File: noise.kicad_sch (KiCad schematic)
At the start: 23 parts, among them J2 Conn_01x04_Pin, SW1 SW_SP3T, U20 LF351N, U5 MM5837

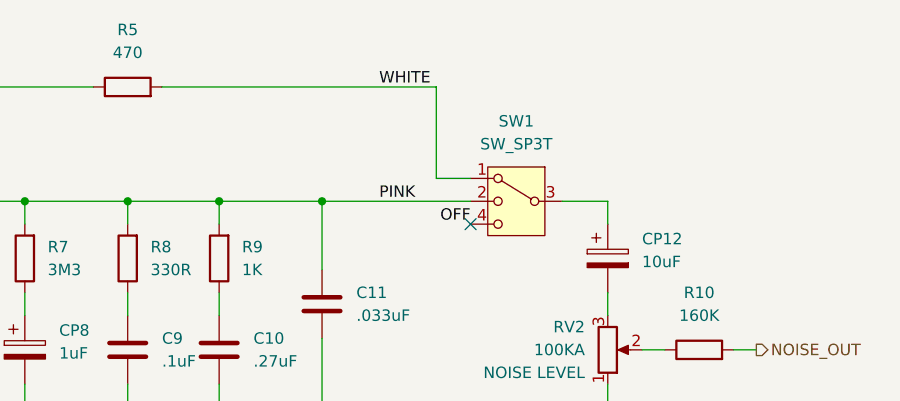
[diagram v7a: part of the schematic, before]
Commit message: Fix VCF layout, routing, adding pads for switches
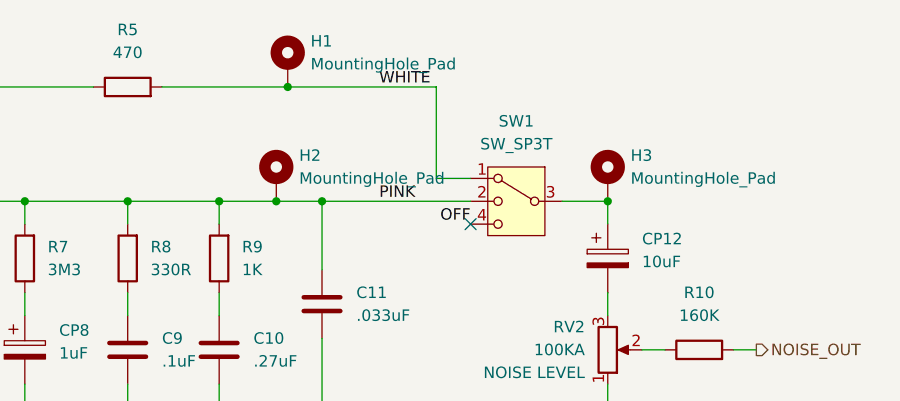
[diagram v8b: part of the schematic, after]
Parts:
- added H1, H2, H3: MountingHole_Pad, MountingHole:MountingHole_2.2mm_M2_Pad, symbol Mechanical:MountingHole_Pad
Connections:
- net PINK: now also H2.1
- net WHITE: now also H1.1
- net at CP12.1, SW1.3: now also H3.1
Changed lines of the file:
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@@
 	)
 	(junction
+		(at 160.02 87.63)
+		(diameter 0)
+		(color 0 0 0 0)
+	)
+	(junction
 		(at 101.6 77.47)
 		(diameter 0)
@@
 	)
 	(junction
+		(at 161.29 74.93)
+		(diameter 0)
+		(color 0 0 0 0)
+	)
+	(junction
 		(at 153.67 87.63)
 		(diameter 0)
@@
 	)
 	(junction
+		(at 196.85 87.63)
+		(diameter 0)
+		(color 0 0 0 0)
+	)
+	(junction
 		(at 132.08 87.63)
 		(diameter 0)
@@
 	(wire
 		(pts
+			(xy 160.02 87.63) (xy 165.1 87.63)
+		)
+		(stroke
+			(width 0)
+			(type default)
+		)
+	)
+	(wire
+		(pts
 			(xy 88.9 83.82) (xy 91.44 83.82)
 		)
@@
 	(wire
 		(pts
-			(xy 153.67 87.63) (xy 165.1 87.63)
+			(xy 153.67 87.63) (xy 160.02 87.63)
 		)
 		(stroke
@@
 	(wire
 		(pts
+			(xy 161.29 74.93) (xy 147.32 74.93)
+		)
+		(stroke
+			(width 0)
+			(type default)
+		)
+	)
+	(wire
+		(pts
 			(xy 143.51 97.79) (xy 143.51 100.33)
 		)
@@
 	(wire
 		(pts
-			(xy 177.8 74.93) (xy 147.32 74.93)
+			(xy 177.8 74.93) (xy 161.29 74.93)
 		)
 		(stroke
@@
 	)
 	(symbol
+		(lib_id "Mechanical:MountingHole_Pad")
+		(at 196.85 85.09 0)
+		(unit 1)
+		(exclude_from_sim no)
+		(in_bom no)
+		(on_board yes)
+		(dnp no)
+		(fields_autoplaced yes)
+		(property "Reference" "H3"
+			(at 199.39 82.5499 0)
+			(effects
+				(font
+					(size 1.27 1.27)
+				)
+				(justify left)
+			)
+		)
+		(property "Value" "MountingHole_Pad"
+			(at 199.39 85.0899 0)
+			(effects
+				(font
+					(size 1.27 1.27)
+				)
+				(justify left)
+			)
+		)
+		(property "Footprint" "MountingHole:MountingHole_2.2mm_M2_Pad"
+			(at 196.85 85.09 0)
+			(effects
+				(font
+					(size 1.27 1.27)
+				)
+				(hide yes)
+			)
+		)
+		(property "Datasheet" "~"
+			(at 196.85 85.09 0)
+			(effects
+				(font
+					(size 1.27 1.27)
+				)
+				(hide yes)
+			)
+		)
+		(property "Description" "Mounting Hole with connection"
+			(at 196.85 85.09 0)
+			(effects
+				(font
+					(size 1.27 1.27)
+				)
+				(hide yes)
+			)
+		)
+		(pin "1"
+		)
+		(instances
+			(project "jensx1000"
+				(path "/3c53febc-5769-4c45-8f8f-0aba2c04e944/23ff179f-f3ca-4876-91dc-9a0adb7dbeaf"
+					(reference "H3")
+					(unit 1)
+				)
+			)
+		)
+	)
+	(symbol
 		(lib_id "Switch:SW_SP3T")
 		(at 186.69 87.63 0)
@@
 					(unit 1)
 				)
+			)
+		)
+	)
+	(symbol
+		(lib_id "Mechanical:MountingHole_Pad")
+		(at 160.02 85.09 0)
+		(unit 1)
+		(exclude_from_sim no)
+		(in_bom no)
+		(on_board yes)
+		(dnp no)
+		(fields_autoplaced yes)
+		(property "Reference" "H2"
+			(at 162.56 82.5499 0)
+			(effects
+				(font
+					(size 1.27 1.27)
+				)
+				(justify left)
+			)
+		)
+		(property "Value" "MountingHole_Pad"
+			(at 162.56 85.0899 0)
+			(effects
+				(font
+					(size 1.27 1.27)
+				)
+				(justify left)
+			)
+		)
+		(property "Footprint" "MountingHole:MountingHole_2.2mm_M2_Pad"
+			(at 160.02 85.09 0)
+			(effects
+				(font
+					(size 1.27 1.27)
+				)
+				(hide yes)
+			)
+		)
+		(property "Datasheet" "~"
+			(at 160.02 85.09 0)
+			(effects
+				(font
+					(size 1.27 1.27)
+				)
+				(hide yes)
+			)
+		)
+		(property "Description" "Mounting Hole with connection"
+			(at 160.02 85.09 0)
+			(effects
+				(font
+					(size 1.27 1.27)
+				)
+				(hide yes)
+			)
+		)
+		(pin "1"
+		)
+		(instances
+			(project "jensx1000"
+				(path "/3c53febc-5769-4c45-8f8f-0aba2c04e944/23ff179f-f3ca-4876-91dc-9a0adb7dbeaf"
+					(reference "H2")
+					(unit 1)
+				)
+			)
+		)
+	)
+	(symbol
+		(lib_id "Mechanical:MountingHole_Pad")
+		(at 161.29 72.39 0)
+		(unit 1)
+		(exclude_from_sim no)
+		(in_bom no)
+		(on_board yes)
+		(dnp no)
+		(fields_autoplaced yes)
+		(property "Reference" "H1"
+			(at 163.83 69.8499 0)
+			(effects
+				(font
+					(size 1.27 1.27)
+				)
+				(justify left)
+			)
+		)
+		(property "Value" "MountingHole_Pad"
+			(at 163.83 72.3899 0)
+			(effects
+				(font
+					(size 1.27 1.27)
+				)
+				(justify left)
+			)
+		)
+		(property "Footprint" "MountingHole:MountingHole_2.2mm_M2_Pad"
+			(at 161.29 72.39 0)
+			(effects
+				(font
+					(size 1.27 1.27)
+				)
+				(hide yes)
+			)
+		)
+		(property "Datasheet" "~"
+			(at 161.29 72.39 0)
+			(effects
+				(font
+					(size 1.27 1.27)
+				)
+				(hide yes)
+			)
+		)
+		(property "Description" "Mounting Hole with connection"
+			(at 161.29 72.39 0)
+			(effects
+				(font
+					(size 1.27 1.27)
+				)
+				(hide yes)
+			)
+		)
+		(pin "1"
+		)
+		(instances
+			(project ""
+				(path "/3c53febc-5769-4c45-8f8f-0aba2c04e944/23ff179f-f3ca-4876-91dc-9a0adb7dbeaf"
+					(reference "H1")
+					(unit 1)
+				)
